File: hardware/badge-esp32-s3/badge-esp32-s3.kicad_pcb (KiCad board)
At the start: 2 copper layers, 131.5 x 83.5 mm, 161 parts, among them CN1 B4B-PH-SM4-TB (LF)(SN), CN3 HDR-TH_2P-P2.54-V-F, J1 Connector, USB-TYPE-C-16P, J10 Conn_01x02_Socket, J2 Connector, USB-TYPE-C-16P, J3 Conn_01x02_Socket, J4 Conn_01x02_Socket, J5 Conn_01x02_Socket, J6 Conn_01x04_Socket, J7 Conn_01x02_Socket, J8 Conn_01x04_Socket, J9 Conn_01x02_Socket, P1 PH-2A_C2319, P2 FPC 0.5MM 12P Pull type H2.0m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, Q1 SS8050 200-350, Q2 SS8050 200-350, Q3 HL2301A, Q5 DTC114E, SW1 TS-1088-AR02016, SW2 TS-1088-AR02016, SW3 SK-12F04-G050, SW7 TS665CJ, SW8 TS665CJ, U1 ESP32-S3-MINI-1-N8, U18 MMA8452QR1_C11360, U19 FH2.54-09-02PZD, U2 NCP167BMX330TBG, U20 2x14_female, U3 CP2102N-A02-GQFN28R, U4 TP4056, U5 TPS63061DSCR, U6 ZX-SH1.0-4PWT

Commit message: try again pls
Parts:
- moved G*** 3.40 mm to (110.5, 142.5)
- moved CN2 2.04 mm to (118.5, 138.7)
- moved CN3 2.04 mm to (115.2, 138.8)
- moved U14 2.04 mm to (124.0, 138.7)
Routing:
- net /GPIO39: track 148.5 -> 0.00 mm, vias 8 -> 0
- net /GPIO42: track 141.4 -> 0.00 mm, vias 2 -> 0
- net /RGBGreenMid: track 136.3 -> 0.00 mm, vias 2 -> 0
- net /GPIO10: track 120.5 -> 0.00 mm, vias 1 -> 0
- net /U0RX: track 120.0 -> 0.00 mm, vias 2 -> 0
- net /LEDSingleMid: track 117.6 -> 0.00 mm, vias 2 -> 0
- net /GPIO41: track 108.4 -> 0.00 mm, vias 2 -> 0
- net /GPIO5: track 106.1 -> 0.00 mm
- net /U0TX: track 105.1 -> 0.00 mm
- net /RGBBlueMid: track 104.2 -> 0.00 mm, vias 2 -> 0
- net /GPIO47: track 190.6 -> 87.6 mm, vias 4 -> 2
- net /BuzzerMid: track 102.2 -> 0.00 mm, vias 2 -> 0
- net /GPIO7: track 99.0 -> 0.00 mm, vias 2 -> 0
- net /GPIO12: track 153.5 -> 56.6 mm, vias 3 -> 2
- net +3.3V: track 368.5 -> 276.0 mm, vias 8 -> 6
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
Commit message: Updated power label.
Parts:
- renumbered SW3 to Power
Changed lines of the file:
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@@
 		(layer "F.Cu")
 		(at 211.5 96.5 90)
-		(property "Reference" "SW3"
+		(property "Reference" "Power"
 			(at 0 -4 90)
 			(layer "F.SilkS")

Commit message: reversed_labels_and_pcb
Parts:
- removed MB2: MiniBadge_Full, minibadge:MiniBadge_Full_NoEdges
- renumbered Power to SW3, BtnL to SW4, BtnU to SW5, BtnR to SW6, BtnD to SW9
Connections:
- P1 pad 1: GND -> /Charging/VBATT
- P1 pad 2: /Charging/VBATT -> GND
- S1 pad X: /JoystickXMid -> /Onboard Peripheral/Joystick/Yout(analog)
- S1 pad Y: /JoystickYMid -> /Onboard Peripheral/Joystick/Xout(analog)
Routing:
- net /Charging/VBATT: track 24.8 -> 21.2 mm
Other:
- board text added: "(+)"
- board text added: "(-)"
- board text removed: "+"
- board text removed: "-"

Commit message: Added boot and reset labels for buttons.
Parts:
- renumbered SW1 to BOOT, SW2 to RESET
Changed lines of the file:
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@@
 		(layer "F.Cu")
 		(at 133.5 72)
-		(property "Reference" "SW1"
+		(property "Reference" "BOOT"
 			(at 0 -2.5 0)
 			(layer "F.SilkS")
@@
 		(layer "F.Cu")
 		(at 164.5 72 180)
-		(property "Reference" "SW2"
+		(property "Reference" "RESET"
 			(at 0 2.5 0)
 			(layer "F.SilkS")

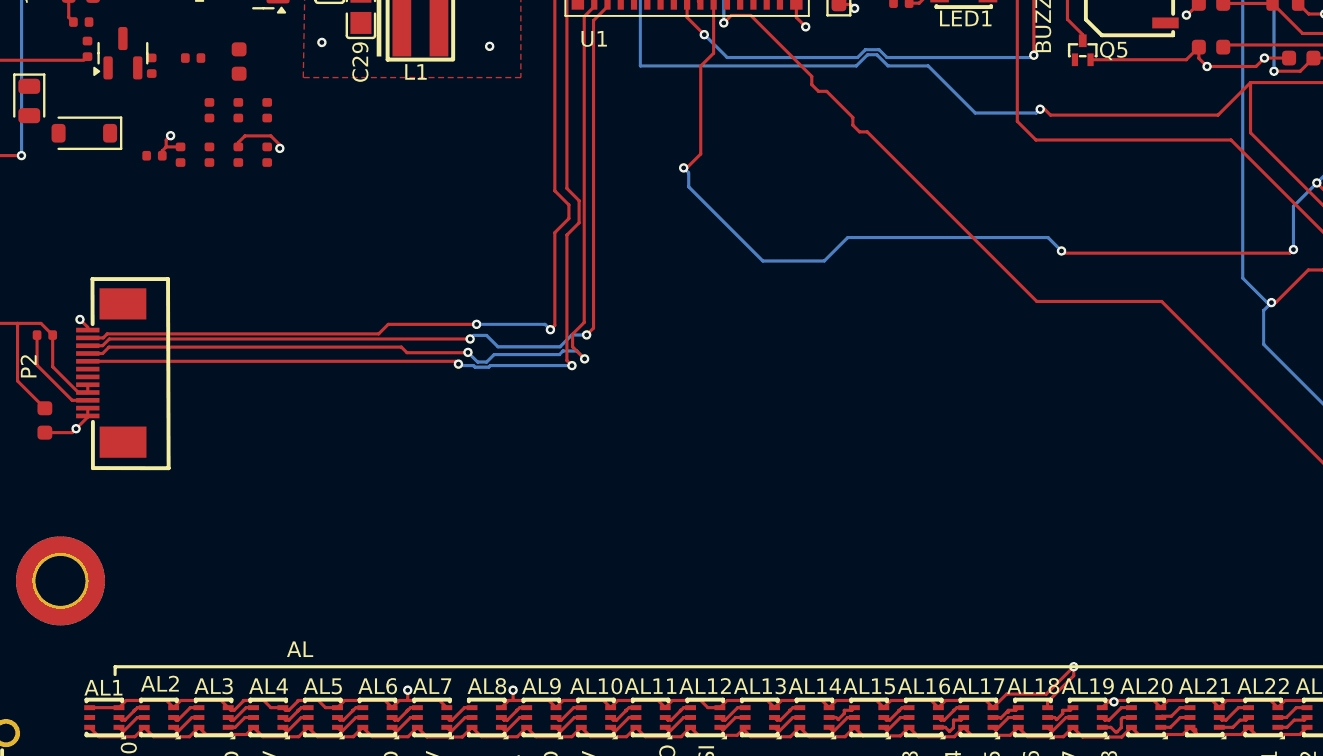
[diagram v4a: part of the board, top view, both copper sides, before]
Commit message: Add Display Silkscreen
See Summary
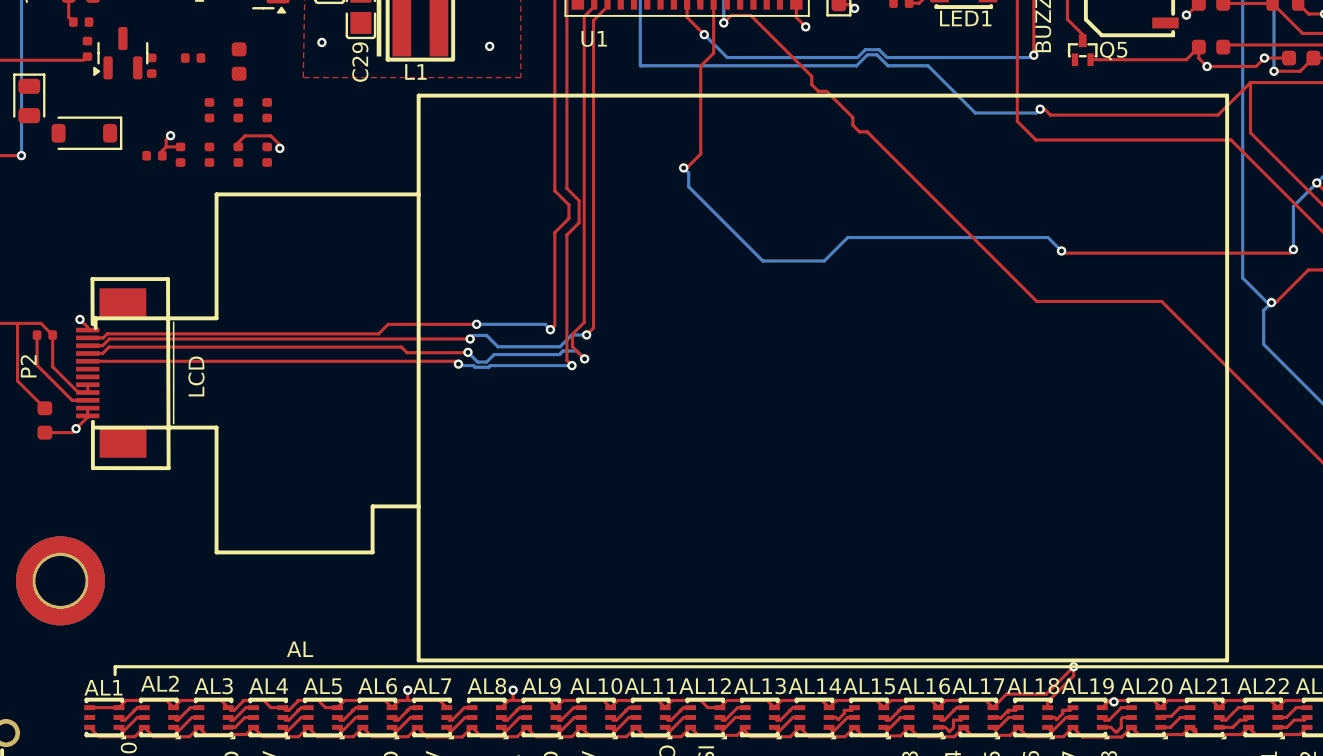
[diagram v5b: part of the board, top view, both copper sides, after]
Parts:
- added LCD: OLED-SMD_HS20HS072RX, lcsc-lib:OLED-SMD_HS20HS072RX, F.Cu at (115.2, 108.9)
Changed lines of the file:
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@@
 		)
+	)
+	(footprint "lcsc-lib:OLED-SMD_HS20HS072RX"
+		(layer "F.Cu")
+		(at 115.25 108.925 -90)
+		(property "Reference" "LCD"
+			(at 0 -4 90)
+			(layer "F.SilkS")
+			(effects
+				(font
+					(size 1 1)
+					(thickness 0.15)
+				)
+			)
+		)
+		(property "Value" "OLED-SMD_HS20HS072RX"
+			(at 0 4 90)
+			(layer "F.Fab")
+			(effects
+				(font
+					(size 1 1)
+					(thickness 0.15)
+				)
+			)
+		)
+		(property "Datasheet" ""
+			(at 0 0 90)
+			(layer "F.Fab")
+			(hide yes)
+			(effects
+				(font
+					(size 1.27 1.27)
+					(thickness 0.15)
+				)
+			)
+		)
+		(property "Description" ""
+			(at 0 0 90)
+			(layer "F.Fab")
+			(hide yes)
+			(effects
+				(font
+					(size 1.27 1.27)
+					(thickness 0.15)
+				)
+			)
+		)
+		(attr through_hole)
+		(fp_line
+			(start -3.75 2.5)
+			(end -3.13 2.5)
+			(stroke
+				(width 0.25)
+				(type solid)
+			)
+			(layer "F.SilkS")
+		)
+		(fp_line
+			(start -3.75 2.5)
+			(end -3.75 -5.25)
+			(stroke
+				(width 0.25)
+				(type solid)
+			)
+			(layer "F.SilkS")
+		)
+		(fp_line
+			(start 3.25 2.5)
+			(end 3.25 -5.25)
+			(stroke
+				(width 0.25)
+				(type solid)
+			)
+			(layer "F.SilkS")
+		)
+		(fp_line
+			(start -3.5 -2.5)
+			(end 3 -2.5)
+			(stroke
+				(width 0.1)
+				(type default)
+			)
+			(layer "F.SilkS")
+		)
+		(fp_line
+			(start -11.69 -5.25)
+			(end -11.69 -18.2)
+			(stroke
+				(width 0.25)
+				(type solid)
+			)
+			(layer "F.SilkS")
+		)
+		(fp_line
+			(start -3.75 -5.25)
+			(end -11.69 -5.25)
+			(stroke
+				(width 0.25)
+				(type solid)
+			)
+			(layer "F.SilkS")
+		)
+		(fp_line
+			(start 3.25 -5.25)
+			(end 11.25 -5.25)
+			(stroke
+				(width 0.25)
+				(type solid)
+			)
+			(layer "F.SilkS")
+		)
+		(fp_line
+			(start 11.25 -5.25)
+			(end 11.25 -15.25)
+			(stroke
+				(width 0.25)
+				(type solid)
+			)
+			(layer "F.SilkS")
+		)
+		(fp_line
+			(start 8.3 -15.25)
+			(end 8.3 -18.2)
+			(stroke
+				(width 0.25)
+				(type solid)
+			)
+			(layer "F.SilkS")
+		)
+		(fp_line
+			(start 11.25 -15.25)
+			(end 8.3 -15.25)
+			(stroke
+				(width 0.25)
+				(type solid)
+			)
+			(layer "F.SilkS")
+		)
+		(fp_line
+			(start -18.02 -18.2)
+			(end 18.17 -18.2)
+			(stroke
+				(width 0.25)
+				(type solid)
+			)
+			(layer "F.SilkS")
+		)
+		(fp_line
+			(start 18.17 -18.2)
+			(end 18.17 -70)
+			(stroke
+				(width 0.25)
+				(type solid)
+			)
+			(layer "F.SilkS")
+		)
+		(fp_line
+			(start -18.02 -70)
+			(end -18.02 -18.2)
+			(stroke
+				(width 0.25)
+				(type solid)
+			)
+			(layer "F.SilkS")
+		)
+		(fp_line
+			(start 18.17 -70)
+			(end -18.02 -70)
+			(stroke
+				(width 0.25)
+				(type solid)
+			)
+			(layer "F.SilkS")
+		)
+		(fp_circle
+			(center -18.03 2.5)
+			(end -18 2.5)
+			(stroke
+				(width 0.06)
+				(type solid)
+			)
+			(fill no)
+			(layer "F.Fab")
+		)
+		(fp_text user "${REFERENCE}"
+			(at 0 0 90)
+			(layer "F.Fab")
+			(effects
+				(font
+					(size 1 1)
+					(thickness 0.15)
+				)
+			)
+		)
+		(embedded_fonts no)
 	)
 	(footprint "PCM_JLCPCB:R_0603"

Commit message: I don't know what changed but I am pushing.
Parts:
- moved CN2 0.21 mm to (118.2, 138.7)
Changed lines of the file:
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@@
 	(footprint "lcsc-lib:HDR-TH_2P-P2.54-V-F"
 		(layer "F.Cu")
-		(at 118.46 138.73 90)
+		(at 118.25 138.73 90)
 		(property "Reference" "CN2"
 			(at -4.77 -1.5 90)

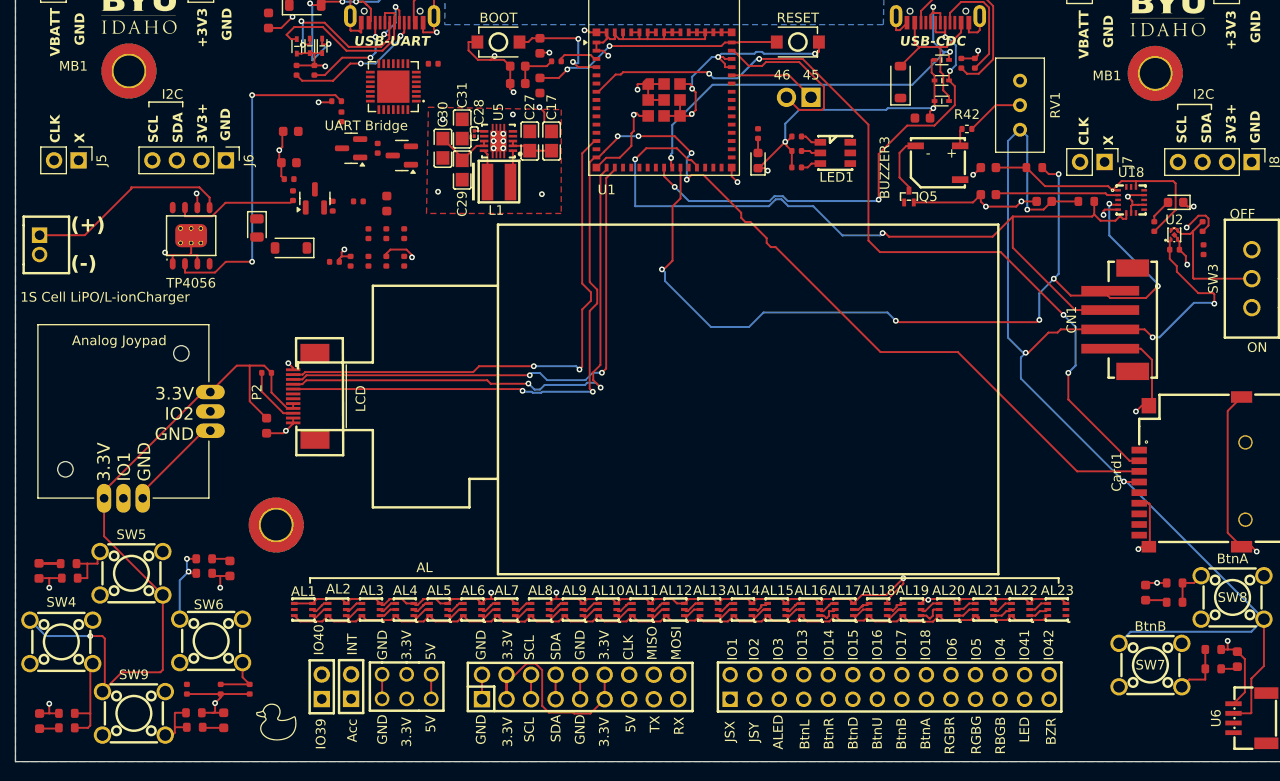
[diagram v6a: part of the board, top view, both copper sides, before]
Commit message: rerouted the gpio pins
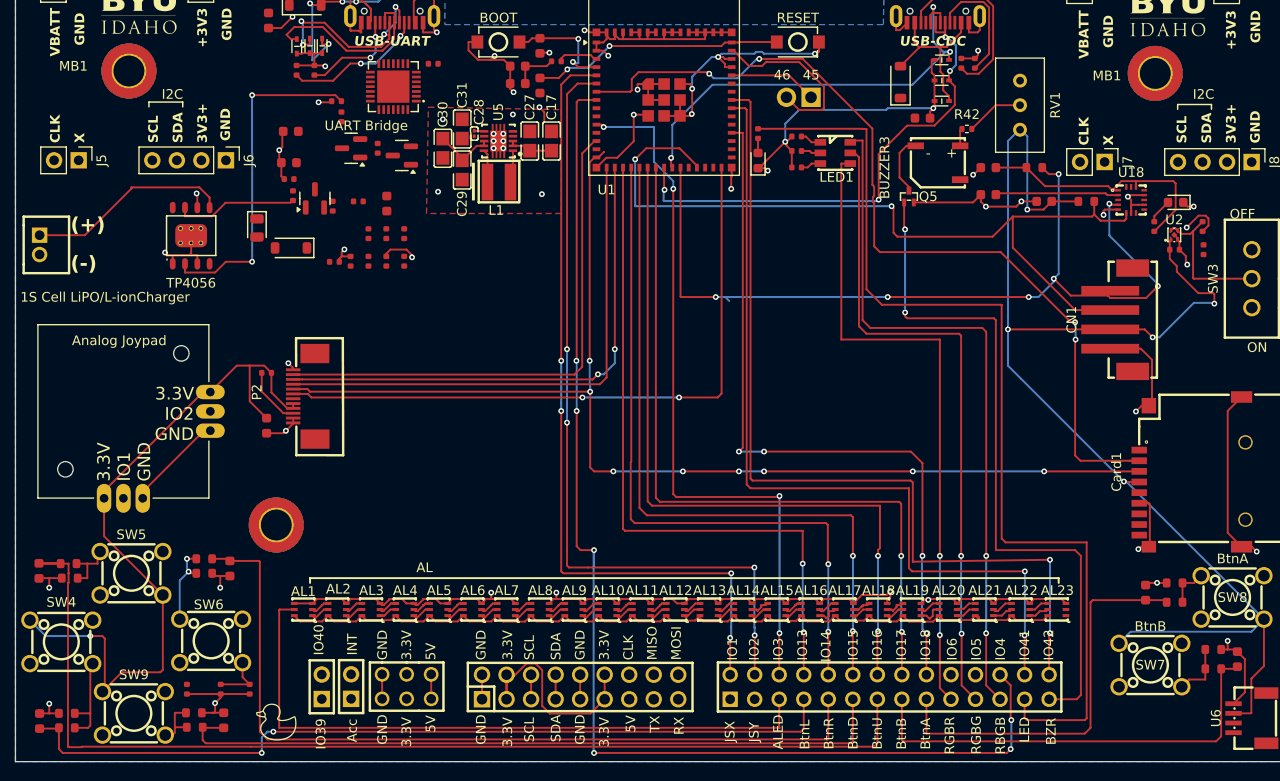
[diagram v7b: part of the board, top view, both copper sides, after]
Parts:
- removed LCD: OLED-SMD_HS20HS072RX, lcsc-lib:OLED-SMD_HS20HS072RX
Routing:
- net /GPIO4: track 0.00 -> 124.8 mm, vias 0 -> 6
- net /UpButtonMid: track 4.00 -> 112.3 mm
- net /LEDSingleMid: track 0.00 -> 102.4 mm
- net /GPIO41: track 0.00 -> 88.6 mm, vias 0 -> 2
- net /RightButtonMid: track 2.03 -> 86.7 mm, vias 0 -> 2
- net /LeftButtonMid: track 2.27 -> 86.3 mm
- net /GPIO2: track 0.00 -> 82.9 mm, vias 0 -> 4
- net /GPIO1: track 0.00 -> 82.8 mm, vias 0 -> 4
- net /GPIO42: track 0.00 -> 78.1 mm, vias 0 -> 2
- net /GPIO18: track 0.00 -> 77.6 mm, vias 0 -> 2
- net /GPIO17: track 0.00 -> 76.2 mm, vias 0 -> 2
- net /GPIO38: track 0.00 -> 75.9 mm, vias 0 -> 4
- net /GPIO7: track 0.00 -> 74.6 mm, vias 0 -> 4
- net /GPIO16: track 0.00 -> 74.3 mm, vias 0 -> 2
- net /DownButtonMid: track 2.20 -> 75.4 mm
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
